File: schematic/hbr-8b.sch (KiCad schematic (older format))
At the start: 29 parts, among them J1 Barrel_Jack, J2 Conn_Coaxial, J3 AudioJack3, Q1 2N3904, SW1 SW_SPDT, SW10 SW_Push, SW2 Rotary_Encoder, SW3 Rotary_Encoder, SW4 SW_SPDT, SW5 SW_Push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

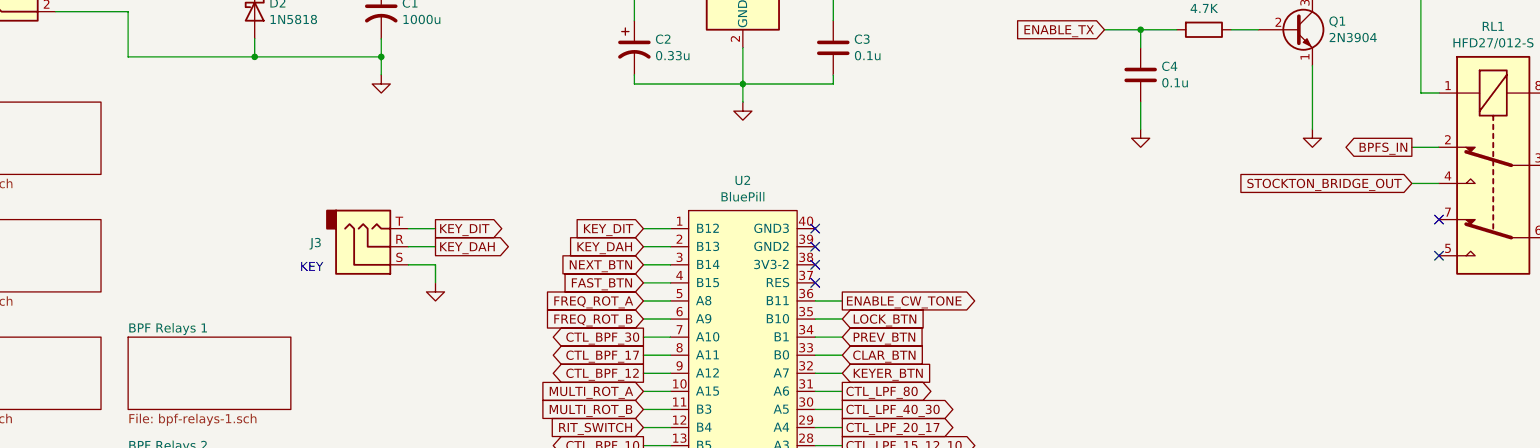
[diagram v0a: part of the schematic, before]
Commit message: Add extra RX filters
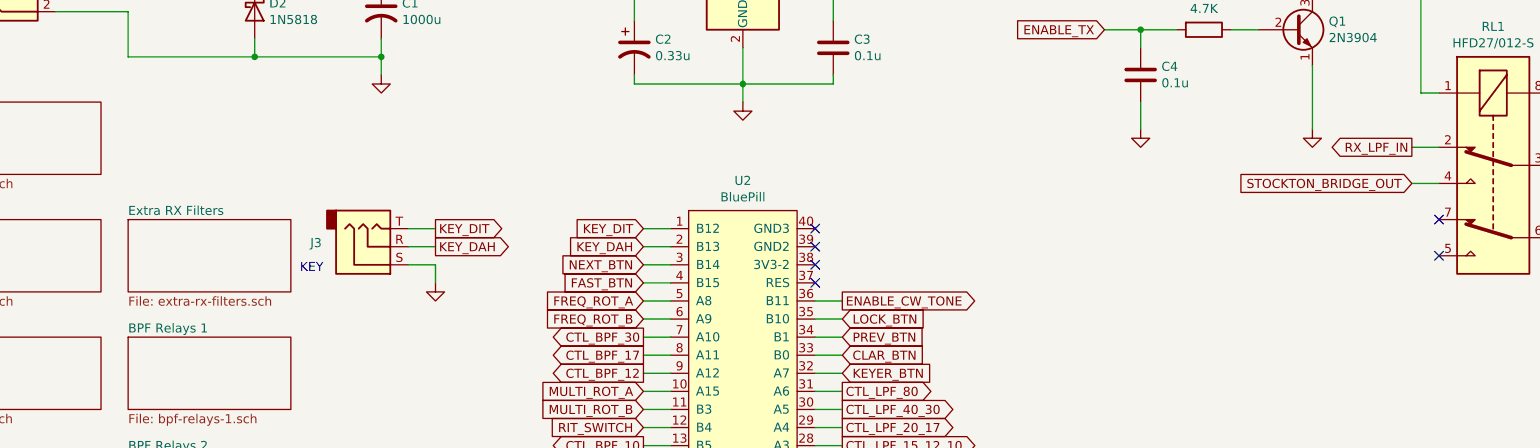
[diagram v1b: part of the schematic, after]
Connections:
- net BPFS_IN renamed RX_LPF_IN
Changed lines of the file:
@@
 $Descr A4 11693 8268
 encoding utf-8
-Sheet 1 13
+Sheet 1 14
 Title "HBR/8B by R2AUK ::: https://eax.me/hbr-8b-transceiver/"
-Date "2022-12-24"
-Rev ""
+Date "2023-01-01"
+Rev "1"
 Comp ""
 Comment1 ""
@@
 $EndComp
 Text GLabel 8900 1950 0    50   Output ~ 0
-BPFS_IN
+RX_LPF_IN
 Text GLabel 8900 2150 0    50   Input ~ 0
 STOCKTON_BRIDGE_OUT
@@
 F1 "bpf-relays-2.sch" 50
 $EndSheet
+$Sheet
+S 1800 2350 900  400
+U 63B3DD40
+F0 "Extra RX Filters" 50
+F1 "extra-rx-filters.sch" 50
+$EndSheet
 $EndSCHEMATC
